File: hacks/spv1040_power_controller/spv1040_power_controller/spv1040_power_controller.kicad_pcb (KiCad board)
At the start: 2 copper layers, 20 parts, among them P1 DC IN, P2 DC OUT, SW1 SWITCH_INV, U1 SPV1040

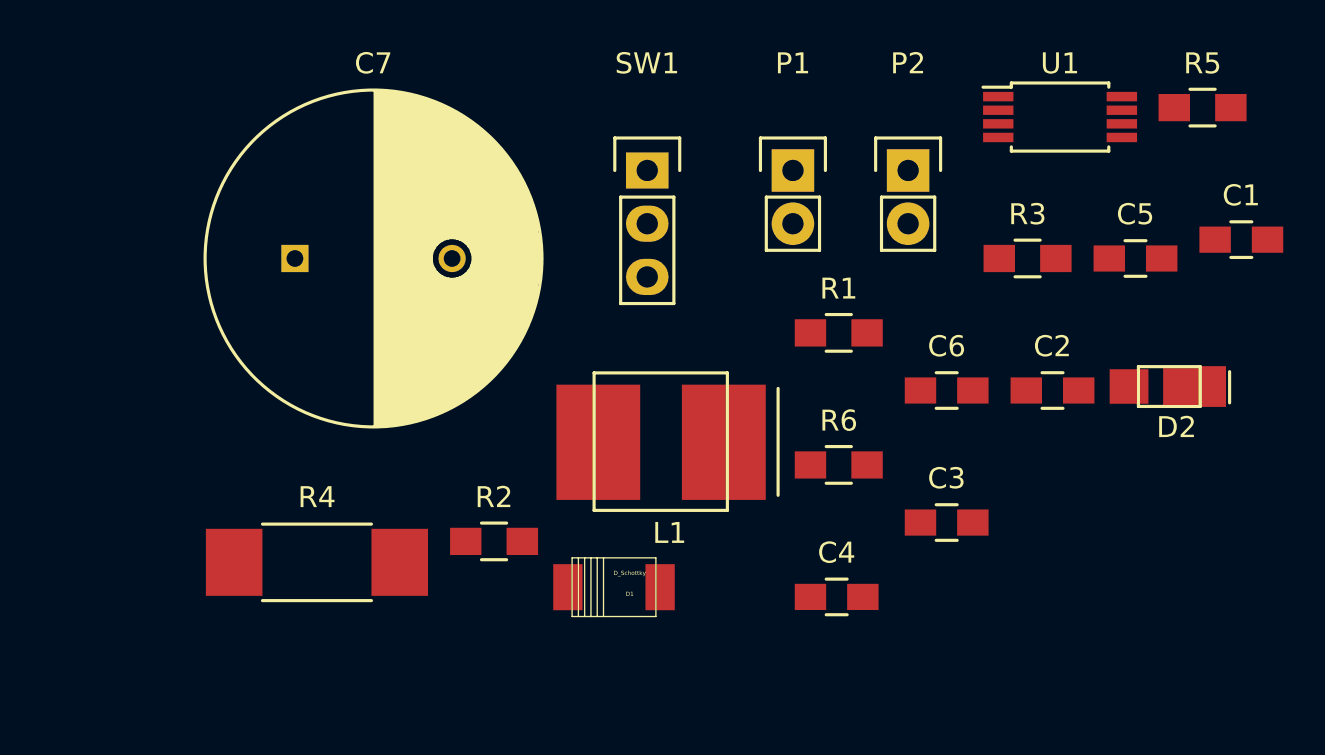
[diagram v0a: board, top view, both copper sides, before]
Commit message: made placement and wiring
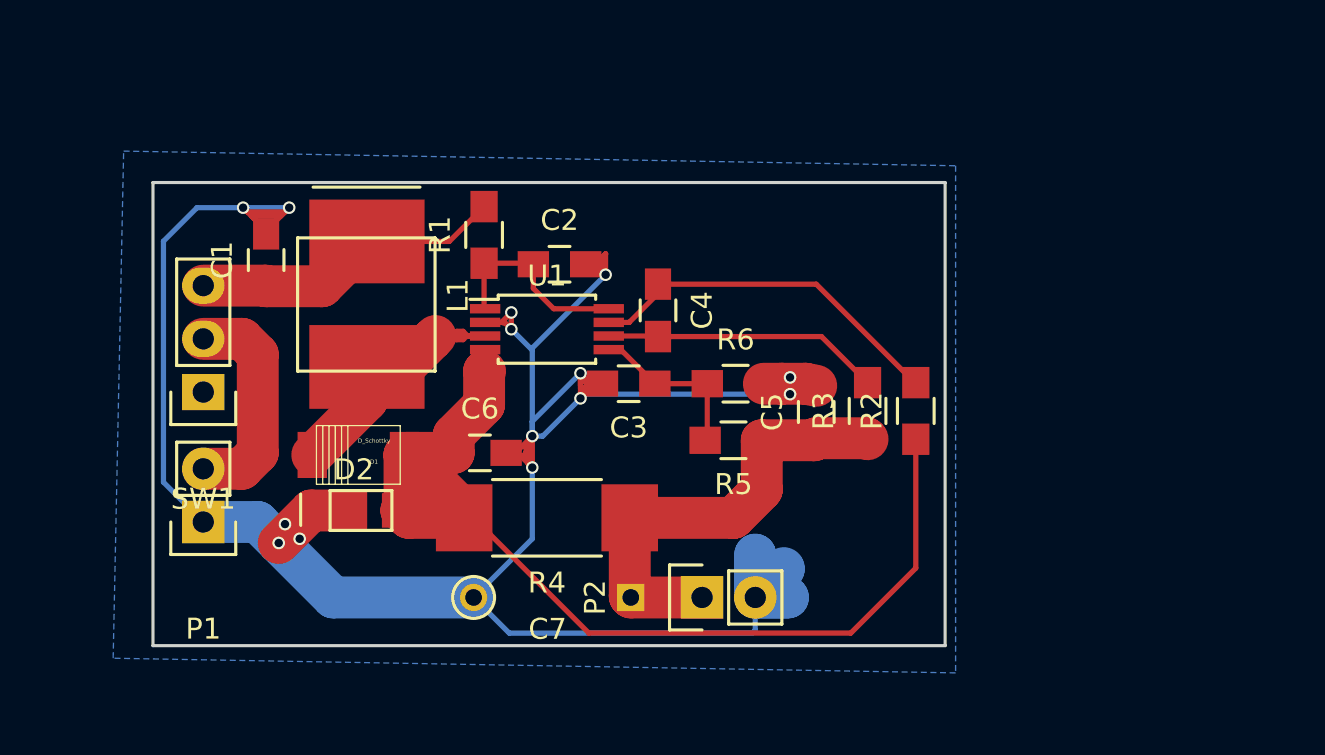
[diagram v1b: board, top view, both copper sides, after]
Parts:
- C7: footprint Capacitors_ThroughHole:C_Radial_D16_L25_P7.5 -> 4700uF_16mm:C_Radial_D16_L25_P7.5
- moved C1 46.5 mm to (165.4, 109.6), turned to 90 degrees
- moved D2 36.5 mm to (171.4, 122.5), turned to 180 degrees
- moved P1 32.8 mm to (162.4, 122.1), turned to 180 degrees
- moved R5 27.4 mm to (187.7, 118.2), turned to 180 degrees
- moved U1 26.5 mm to (178.8, 112.9)
- moved C2 24.3 mm to (179.4, 109.8)
- moved SW1 23.7 mm to (162.4, 115.9), turned to 180 degrees
- moved C7 22.8 mm to (182.8, 125.7), turned to 180 degrees
- moved P2 22.6 mm to (186.2, 125.7), turned to 90 degrees
- moved C6 22.5 mm to (175.6, 118.8)
- moved R2 21.1 mm to (196.4, 116.8), turned to 90 degrees
- moved R1 17.6 mm to (175.8, 108.4), turned to 90 degrees
- moved C5 16.9 mm to (191.7, 116.8), turned to 90 degrees
- moved C3 16.6 mm to (182.7, 115.5), turned to 180 degrees
- moved C4 16.1 mm to (184.1, 112.0), turned to 270 degrees
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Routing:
- net GND: track 0.00 -> 135.1 mm, vias 0 -> 14
- net Net-(C6-Pad1): track 0.00 -> 50.1 mm
- net Net-(C5-Pad1): track 0.00 -> 23.5 mm
- net Net-(D1-Pad2): track 0.00 -> 22.3 mm
- net Net-(C4-Pad1): track 0.00 -> 17.6 mm
- net Net-(C1-Pad1): track 0.00 -> 15.0 mm
- net Net-(C4-Pad2): track 0.00 -> 13.3 mm
- net VCC: track 0.00 -> 10.5 mm
- net Net-(C2-Pad1): track 0.00 -> 9.72 mm
- net Net-(C3-Pad1): track 0.00 -> 8.11 mm
- added copper zone on B.Cu, net GND
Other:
- board outline added: 37.8 x 22.1 mm

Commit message: pcb ready for test
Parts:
- added REF**: MountingHole_2.2mm_M2, Mounting_Holes:MountingHole_2.2mm_M2, F.Cu at (195.0, 108.8)
- D1: value D_Schottky -> D1
- DC IN: renamed from P1
- DC OUT: renamed from P2
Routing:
- net GND: track 135.1 -> 154.2 mm, vias 14 -> 16
- net Net-(C1-Pad1): track 15.0 -> 20.4 mm, vias 0 -> 2
- net Net-(D1-Pad2): track 22.3 -> 25.5 mm, vias 0 -> 2
- added copper zone on F.Cu, net GND
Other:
- board text added: "DC IN"
- board text added: "GND"
- board text added: "Solar cell power controller using SPV1040 by @mik4el4ndersson 2016 V01. DC IN max 3V 1A DC OUT max 5V 100mA"
- board text added: "VCC"

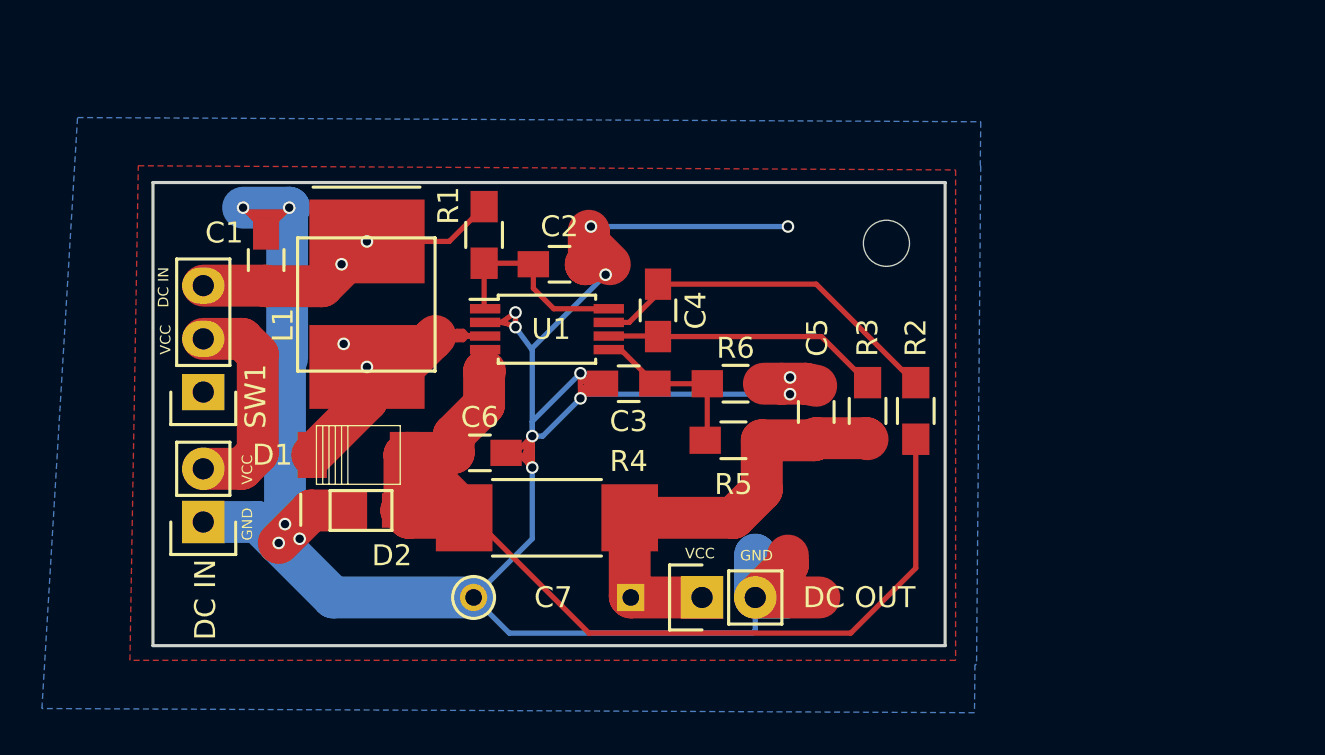
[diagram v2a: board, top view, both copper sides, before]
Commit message: added trim pot to mpp-set
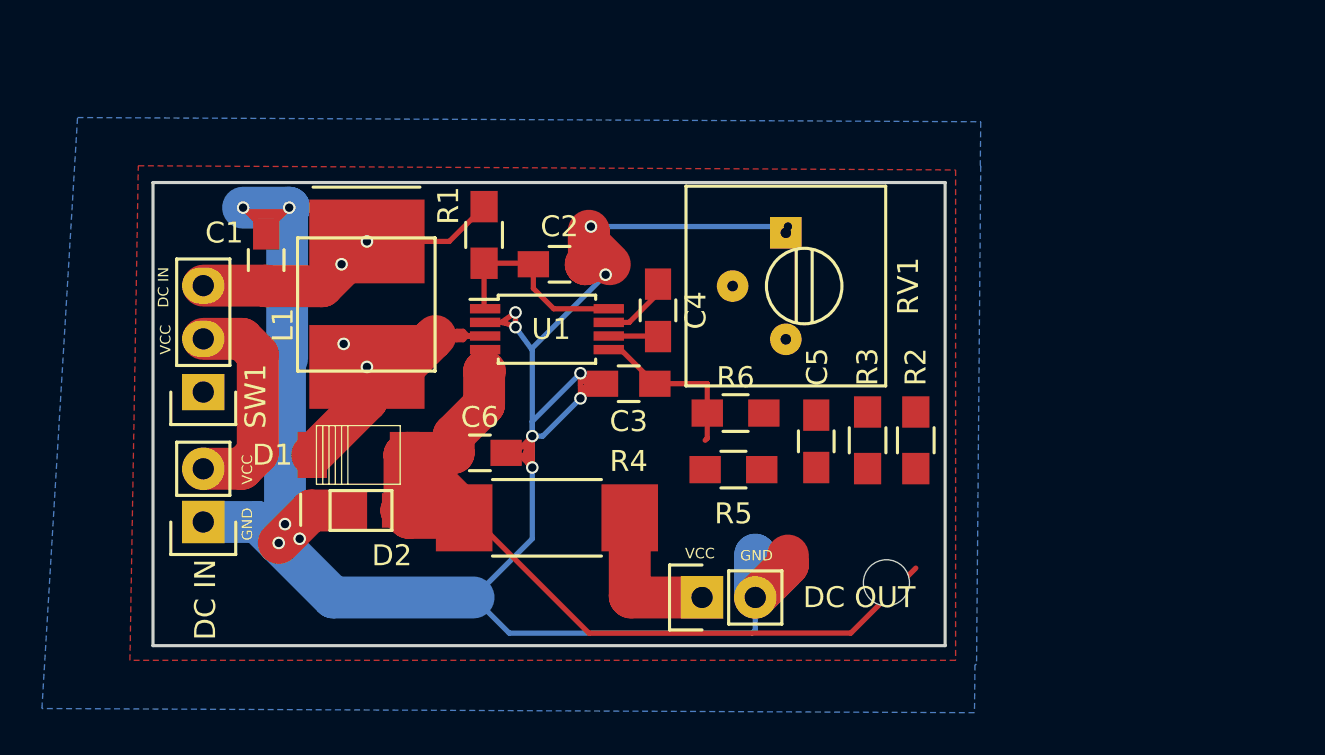
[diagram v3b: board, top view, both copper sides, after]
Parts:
- removed C7: 4700uF, 4700uF_16mm:C_Radial_D16_L25_P7.5
- added RV1: POT, Potentiometers:Potentiometer_Trimmer-Suntan-TSR-3386P, F.Cu at (190.2, 108.3)
- D1: value D1 -> D_Schottky
- moved REF** 16.2 mm to (195.0, 125.0)
- moved C5 1.40 mm to (191.7, 118.2)
- moved R2 1.40 mm to (196.4, 118.2)
- moved R3 1.40 mm to (194.1, 118.2)
- moved R6 1.40 mm to (187.8, 116.9)
- moved R5 1.40 mm to (187.7, 119.6)
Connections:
- R1 pad 1: Net-(C2-Pad1) -> Net-(C1-Pad1)
- R1 pad 2: Net-(C1-Pad1) -> Net-(C2-Pad1)
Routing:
- net GND: track 154.2 -> 72.8 mm, vias 16 -> 4
- net Net-(C1-Pad1): track 20.4 -> 83.1 mm, vias 2 -> 12
- net Net-(C5-Pad1): track 23.5 -> 7.22 mm
- net Net-(C4-Pad1): track 17.6 -> 3.37 mm
- net Net-(C4-Pad2): track 13.3 -> 2.36 mm
- net Net-(C6-Pad1): track 50.1 -> 44.0 mm
- net Net-(C2-Pad1): track 9.72 -> 7.64 mm

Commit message: ordered spv1040 pcb
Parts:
- added C7: 4700uF, 4700uF_16mm:C_Radial_D16_L25_P7.5, F.Cu at (182.4, 126.9)
- moved R2 19.3 mm to (177.2, 116.8), turned to 0 degrees
- moved REF** 16.7 mm to (195.4, 108.3)
- moved C5 15.6 mm to (178.7, 126.9), turned to 180 degrees
- moved RV1 10.5 mm to (192.8, 118.5), turned to 90 degrees
- moved R3 9.63 mm to (186.4, 112.3), turned to 270 degrees
- moved DC OUT 7.21 mm to (193.4, 126.2)
- moved R6 3.77 mm to (184.2, 118.1)
- moved D2 3.54 mm to (168.6, 120.4), turned to 0 degrees
- moved R5 3.52 mm to (184.2, 120.2)
- moved C6 2.04 mm to (175.3, 120.8)
- moved R4 1.93 mm to (178.7, 123.8)
- moved C3 1.52 mm to (184.1, 116.0), turned to 0 degrees
- moved C4 0.43 mm to (184.1, 112.4)
- moved DC IN 0.06 mm to (162.4, 122.0)
- turned R1 to 270 degrees
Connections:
- D2 pad 1: Net-(C6-Pad1) -> GND
- D2 pad 2: GND -> Net-(C6-Pad1)
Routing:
- net Net-(C1-Pad1): track 83.1 -> 48.1 mm, vias 12 -> 2
- net Net-(C5-Pad1): track 7.22 -> 38.0 mm
- net Net-(C6-Pad1): track 44.0 -> 23.6 mm
- net Net-(C4-Pad1): track 3.37 -> 9.06 mm
- net GND: track 72.8 -> 68.3 mm, vias 4 -> 7
- net Net-(C4-Pad2): track 2.36 -> 4.76 mm
- net Net-(C2-Pad1): track 7.64 -> 9.93 mm
- net Net-(C3-Pad1): track 8.11 -> 7.36 mm
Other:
- rule pad_to_mask_clearance: 0.2 -> 0.0508
- board text added: "Solar cell power controller using SPV1040 by @mik4el4ndersson 2016 V01. DC IN max 3V 1A DC OUT max 5V"
- board text removed: "Solar cell power controller using SPV1040 by @mik4el4ndersson 2016 V01. DC IN max 3V 1A DC OUT max 5V 100mA"
